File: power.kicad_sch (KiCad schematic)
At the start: 36 parts, among them Q1 DMN1150UFB-7B, U11 LP5900SDX-1.8/NOPB, U13 TPS746-3.3DRV, U21 NCV8187AMT180TAG, U33 TPS2116DRLR, U6 LMR51420YDDCR, U7 LMR51420YDDCR

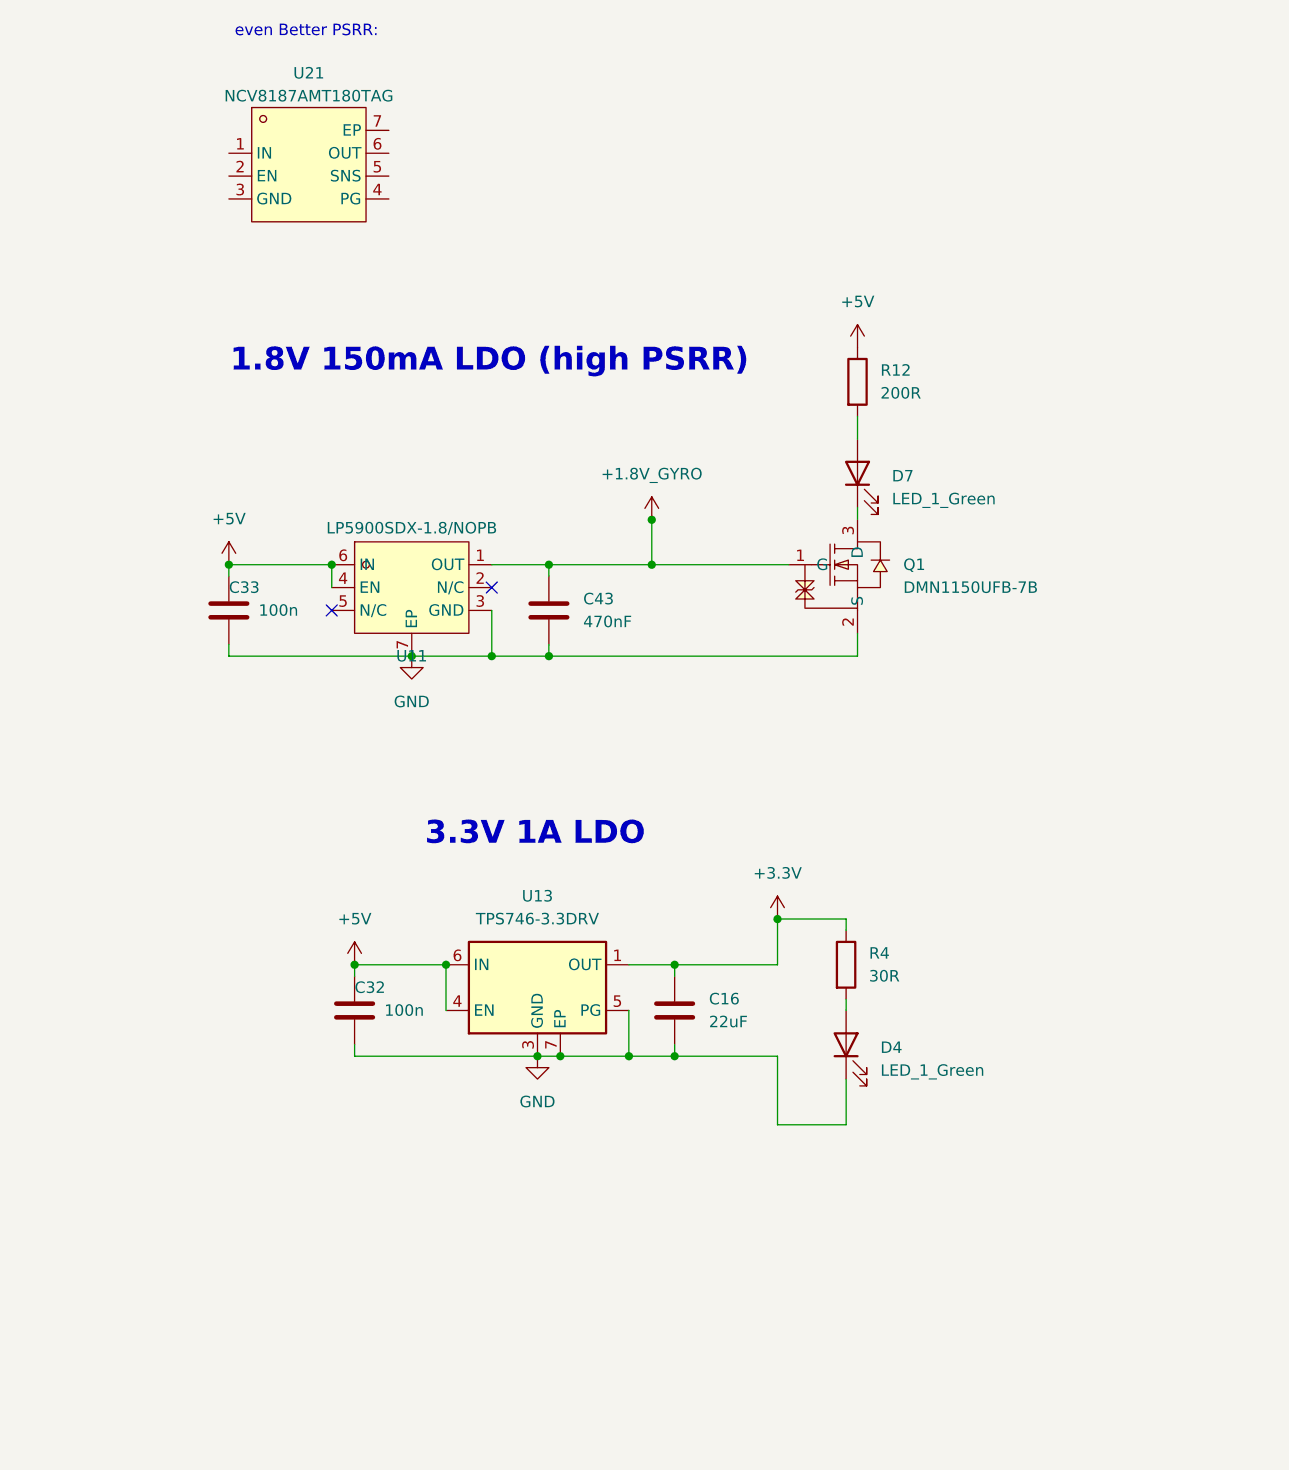
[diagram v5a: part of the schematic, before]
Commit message: Switched to RP2354B for V2 of the FC for more IO. I want to try implement OSD on PIO state machine. I know BF already uses all of them but it should be possible and then later try to combine it witht the WS2812 protocol PIO2. If anybody here has any experience with analog OSD generation let me know, I just want to make a circuit that would allow further software development later. The reason I want to do it this way is it's cheap BOM<1 euro and low footprint, just 2 2x2 IC's and some passives.
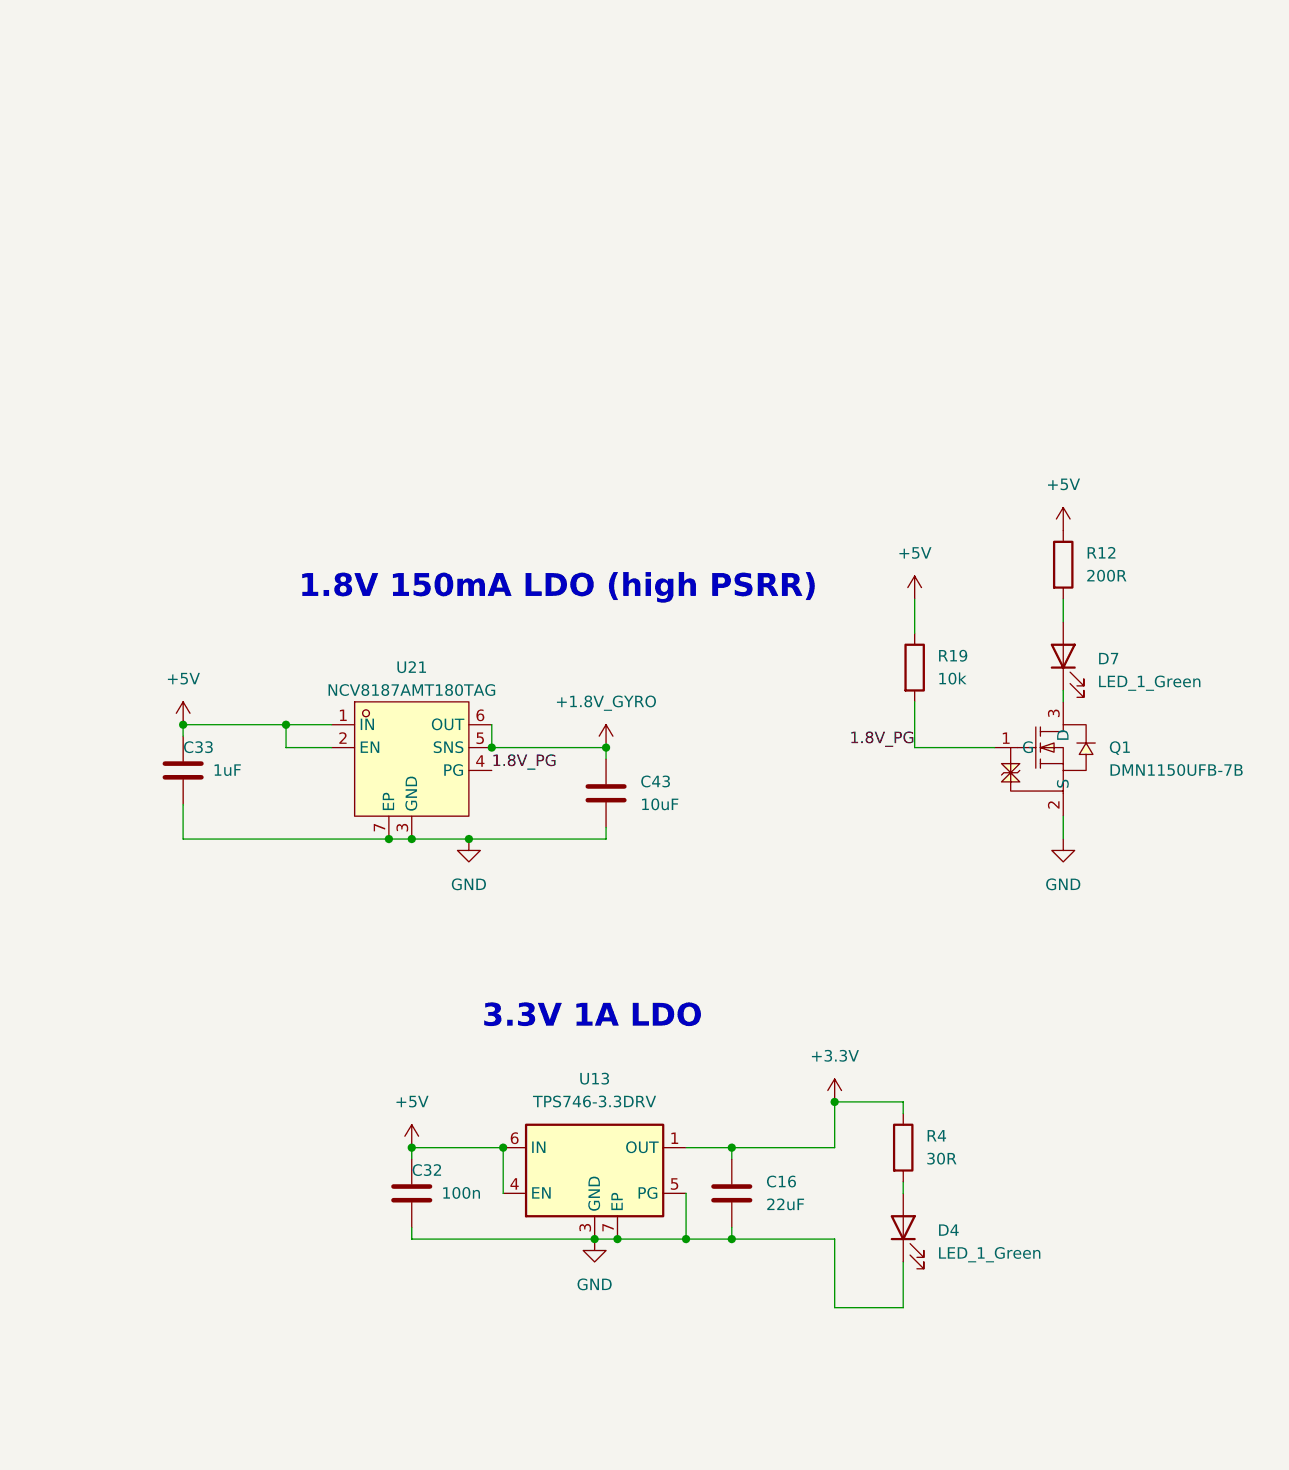
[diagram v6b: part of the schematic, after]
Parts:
- removed U11: LP5900SDX-1.8/NOPB, lib:WSON-6_L2.5-W2.2-P0.65-BL-EP, symbol lib:LP5900SDX-1.8_NOPB
- added R19: 10k, Resistor_SMD:R_0402_1005Metric, symbol Device:R
- C33: value 100n -> 1uF
- C43: value 470nF -> 10uF
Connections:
- net +1.8V_GYRO: now also U21.5 (SNS), U21.6 (OUT); no longer Q1.1 (G)
- net +5V: now also U21.1 (IN), U21.2 (EN), R19.1
- net GND: now also U21.3 (GND), U21.7 (EP)
- net 1.8V_PG: now reaches U21.4 (PG)
- net 1.8V_PG: now also Q1.1 (G), R19.2
- no-connect marks 3 -> 1
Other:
- note removed: "even Better PSRR:"
- moved on the sheet: C16, C32, C33, C43, D4, D7, Q1, R12, R4, U13, U21
